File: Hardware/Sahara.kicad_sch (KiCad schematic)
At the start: 21 parts, among them J1 Conn_01x04, SW1 SW_Push, U1 STM32F103CBT6, Y1 8MHz 18 pF, Y2 32.768 7 pF

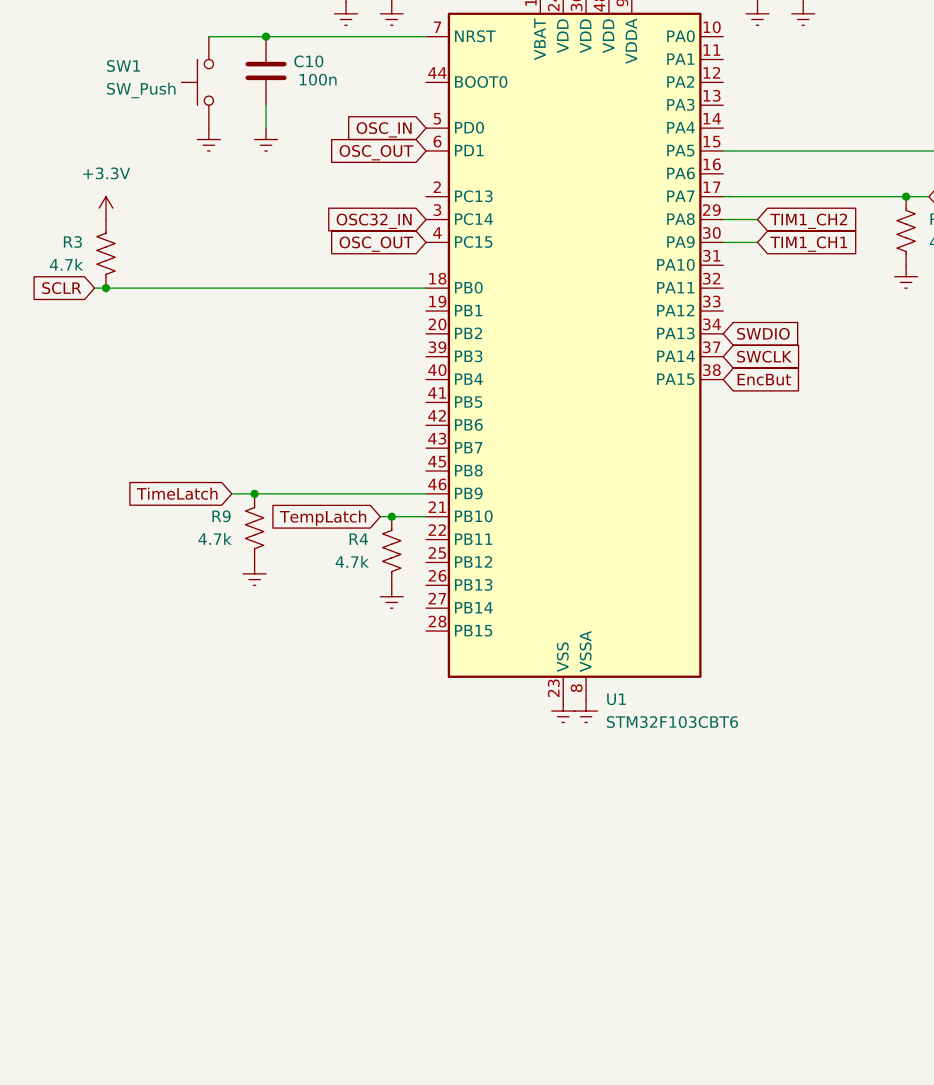
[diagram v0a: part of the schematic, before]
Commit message: schematic update
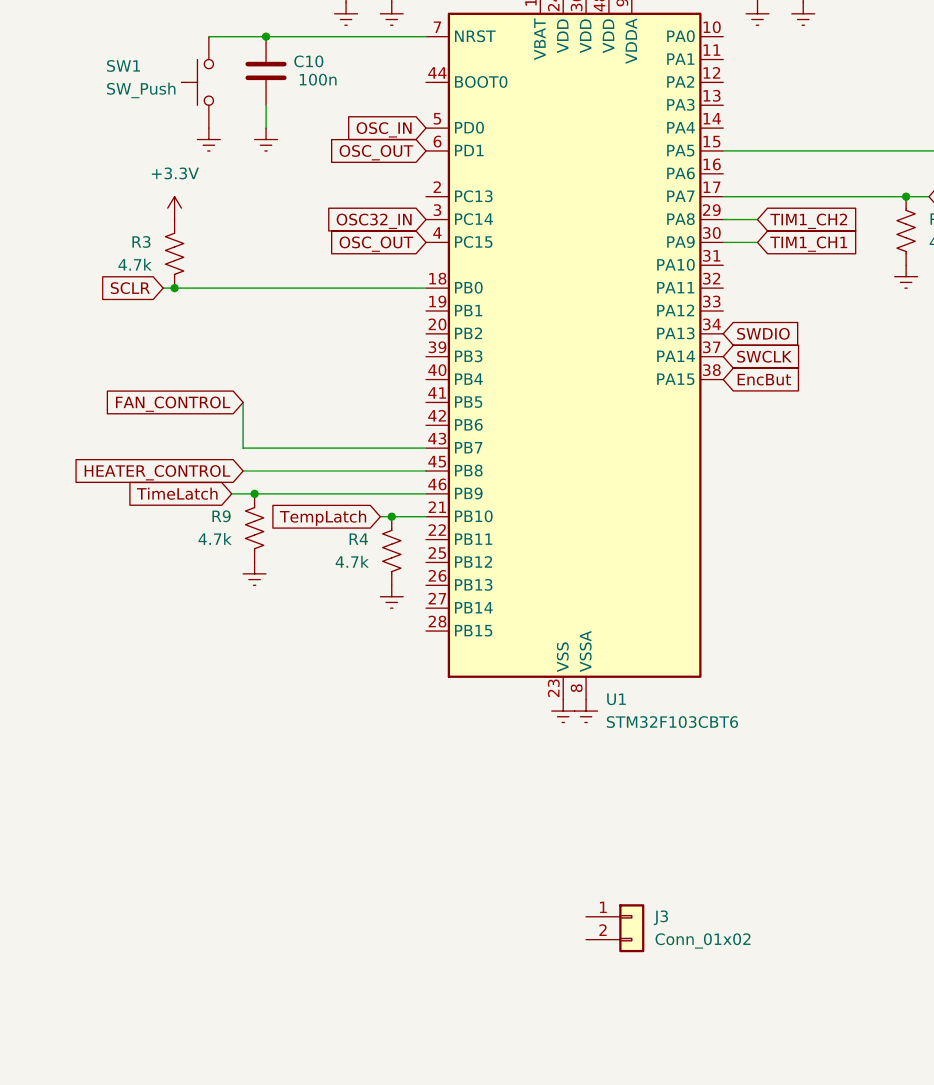
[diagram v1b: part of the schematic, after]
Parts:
- added J3: Conn_01x02, symbol Connector_Generic:Conn_01x02
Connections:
- net FAN_CONTROL: now reaches U1.43 (PB7)
- net HEATER_CONTROL: now reaches U1.45 (PB8)
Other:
- moved on the sheet: R3
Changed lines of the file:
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@@
 	)
 	(junction
-		(at 25.4 76.2)
+		(at 33.02 76.2)
 		(diameter 0)
 		(color 0 0 0 0)
@@
 	(wire
 		(pts
+			(xy 40.64 96.52) (xy 60.96 96.52)
+		)
+		(stroke
+			(width 0)
+			(type default)
+		)
+	)
+	(wire
+		(pts
 			(xy 161.29 30.48) (xy 166.37 30.48)
 		)
@@
 	(wire
 		(pts
-			(xy 24.13 76.2) (xy 25.4 76.2)
+			(xy 31.75 76.2) (xy 33.02 76.2)
 		)
 		(stroke
@@
 	(wire
 		(pts
+			(xy 40.64 93.98) (xy 60.96 93.98)
+		)
+		(stroke
+			(width 0)
+			(type default)
+		)
+	)
+	(wire
+		(pts
 			(xy 166.37 20.32) (xy 177.8 20.32)
 		)
@@
 	(wire
 		(pts
-			(xy 25.4 76.2) (xy 60.96 76.2)
+			(xy 33.02 76.2) (xy 60.96 76.2)
 		)
 		(stroke
@@
 	(wire
 		(pts
+			(xy 40.64 88.9) (xy 40.64 93.98)
+		)
+		(stroke
+			(width 0)
+			(type default)
+		)
+	)
+	(wire
+		(pts
 			(xy 55.88 101.6) (xy 57.15 101.6)
 		)
@@
 	(global_label "SCLR"
 		(shape input)
-		(at 24.13 76.2 180)
+		(at 31.75 76.2 180)
+		(fields_autoplaced yes)
+		(effects
+			(font
+				(size 1.27 1.27)
+			)
+			(justify right)
+		)
+		(property "Intersheetrefs" "${INTERSHEET_REFS}"
+			(at 23.9872 76.2 0)
+			(effects
+				(font
+					(size 1.27 1.27)
+				)
+				(justify right)
+				(hide yes)
+			)
+		)
+	)
+	(global_label "FAN_CONTROL"
+		(shape input)
+		(at 40.64 88.9 180)
 		(fields_autoplaced yes)
 		(effects
@@
 		)
 		(property "Intersheetrefs" "${INTERSHEET_REFS}"
-			(at 16.3672 76.2 0)
+			(at 24.6523 88.9 0)
 			(effects
 				(font
@@
 		)
 	)
+	(global_label "HEATER_CONTROL"
+		(shape input)
+		(at 40.64 96.52 180)
+		(fields_autoplaced yes)
+		(effects
+			(font
+				(size 1.27 1.27)
+			)
+			(justify right)
+		)
+		(property "Intersheetrefs" "${INTERSHEET_REFS}"
+			(at 21.2053 96.52 0)
+			(effects
+				(font
+					(size 1.27 1.27)
+				)
+				(justify right)
+				(hide yes)
+			)
+		)
+	)
 	(global_label "OSC32_IN"
 		(shape input)
@@
 	(symbol
 		(lib_id "Device:R_US")
-		(at 25.4 72.39 0)
+		(at 33.02 72.39 0)
 		(mirror y)
 		(unit 1)
@@
 		(dnp no)
 		(property "Reference" "R3"
-			(at 22.86 71.1199 0)
+			(at 30.48 71.1199 0)
 			(effects
 				(font
@@
 		)
 		(property "Value" "4.7k"
-			(at 22.86 73.6599 0)
+			(at 30.48 73.6599 0)
 			(effects
 				(font
@@
 		)
 		(property "Footprint" ""
-			(at 24.384 72.644 90)
+			(at 32.004 72.644 90)
 			(effects
 				(font
@@
 		)
 		(property "Datasheet" "~"
-			(at 25.4 72.39 0)
+			(at 33.02 72.39 0)
 			(effects
 				(font
@@
 		)
 		(property "Description" "Resistor, US symbol"
-			(at 25.4 72.39 0)
+			(at 33.02 72.39 0)
 			(effects
 				(font
@@
 	(symbol
 		(lib_id "power:+3.3V")
-		(at 25.4 68.58 0)
+		(at 33.02 68.58 0)
 		(unit 1)
 		(exclude_from_sim no)
@@
 		(fields_autoplaced yes)
 		(property "Reference" "#PWR020"
-			(at 25.4 72.39 0)
+			(at 33.02 72.39 0)
 			(effects
 				(font
@@
 		)
 		(property "Value" "+3.3V"
-			(at 25.4 63.5 0)
+			(at 33.02 63.5 0)
 			(effects
 				(font
@@
 		)
 		(property "Footprint" ""
-			(at 25.4 68.58 0)
+			(at 33.02 68.58 0)
 			(effects
 				(font
@@
 		)
 		(property "Datasheet" ""
-			(at 25.4 68.58 0)
+			(at 33.02 68.58 0)
 			(effects
 				(font
@@
 		)
 		(property "Description" "Power symbol creates a global label with name \"+3.3V\""
-			(at 25.4 68.58 0)
+			(at 33.02 68.58 0)
 			(effects
 				(font
@@
 					(unit 1)
 				)
+			)
+		)
+	)
+	(symbol
+		(lib_id "Connector_Generic:Conn_01x02")
+		(at 83.82 146.05 0)
+		(unit 1)
+		(exclude_from_sim no)
+		(in_bom yes)
+		(on_board yes)
+		(dnp no)
+		(fields_autoplaced yes)
+		(property "Reference" "J3"
+			(at 86.36 146.0499 0)
+			(effects
+				(font
+					(size 1.27 1.27)
+				)
+				(justify left)
+			)
+		)
+		(property "Value" "Conn_01x02"
+			(at 86.36 148.5899 0)
+			(effects
+				(font
+					(size 1.27 1.27)
+				)
+				(justify left)
+			)
+		)
+		(property "Footprint" ""
+			(at 83.82 146.05 0)
+			(effects
+				(font
+					(size 1.27 1.27)
+				)
+				(hide yes)
+			)
+		)
+		(property "Datasheet" "~"
+			(at 83.82 146.05 0)
+			(effects
+				(font
+					(size 1.27 1.27)
+				)
+				(hide yes)
+			)
+		)
+		(property "Description" "Generic connector, single row, 01x02, script generated (kicad-library-utils/schlib/autogen/connector/)"
+			(at 83.82 146.05 0)
+			(effects
+				(font
+					(size 1.27 1.27)
+				)
+				(hide yes)
+			)
+		)
+		(pin "1"
+		)
+		(pin "2"
+		)
+		(instances
+			(project ""
+				(path "/1677429e-c497-4bfd-afaa-f24906fcbe1d"
+					(reference "J3")
+					(unit 1)
+				)

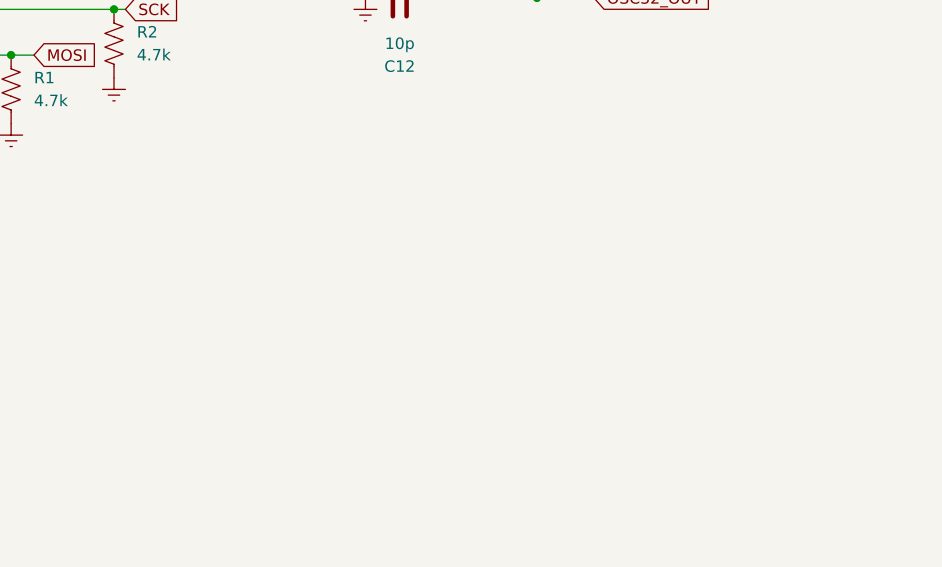
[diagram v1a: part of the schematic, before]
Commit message: Safety features on mains voltage
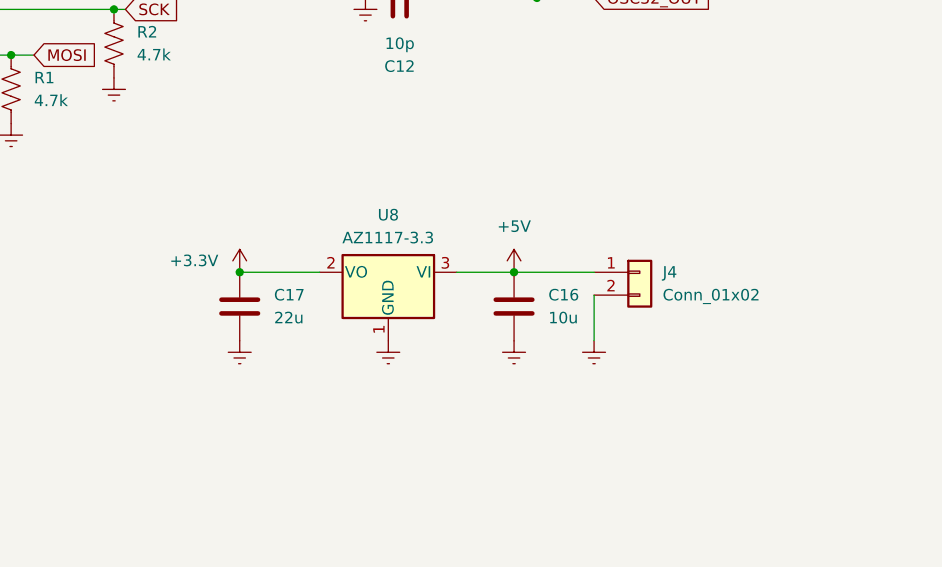
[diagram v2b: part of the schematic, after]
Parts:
- added C16: 10u, symbol Device:C
- added C17: 22u, symbol Device:C
- added J4: Conn_01x02, symbol Connector_Generic:Conn_01x02
- added U8: AZ1117-3.3, symbol Regulator_Linear:AZ1117-3.3
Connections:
- net +3.3V: now also C17.1, U8.2 (VO)
- net Earth: now also C16.2, C17.2, J4.2 (Pin_2), U8.1 (GND)
- new net +5V: C16.1, J4.1 (Pin_1), U8.3 (VI)

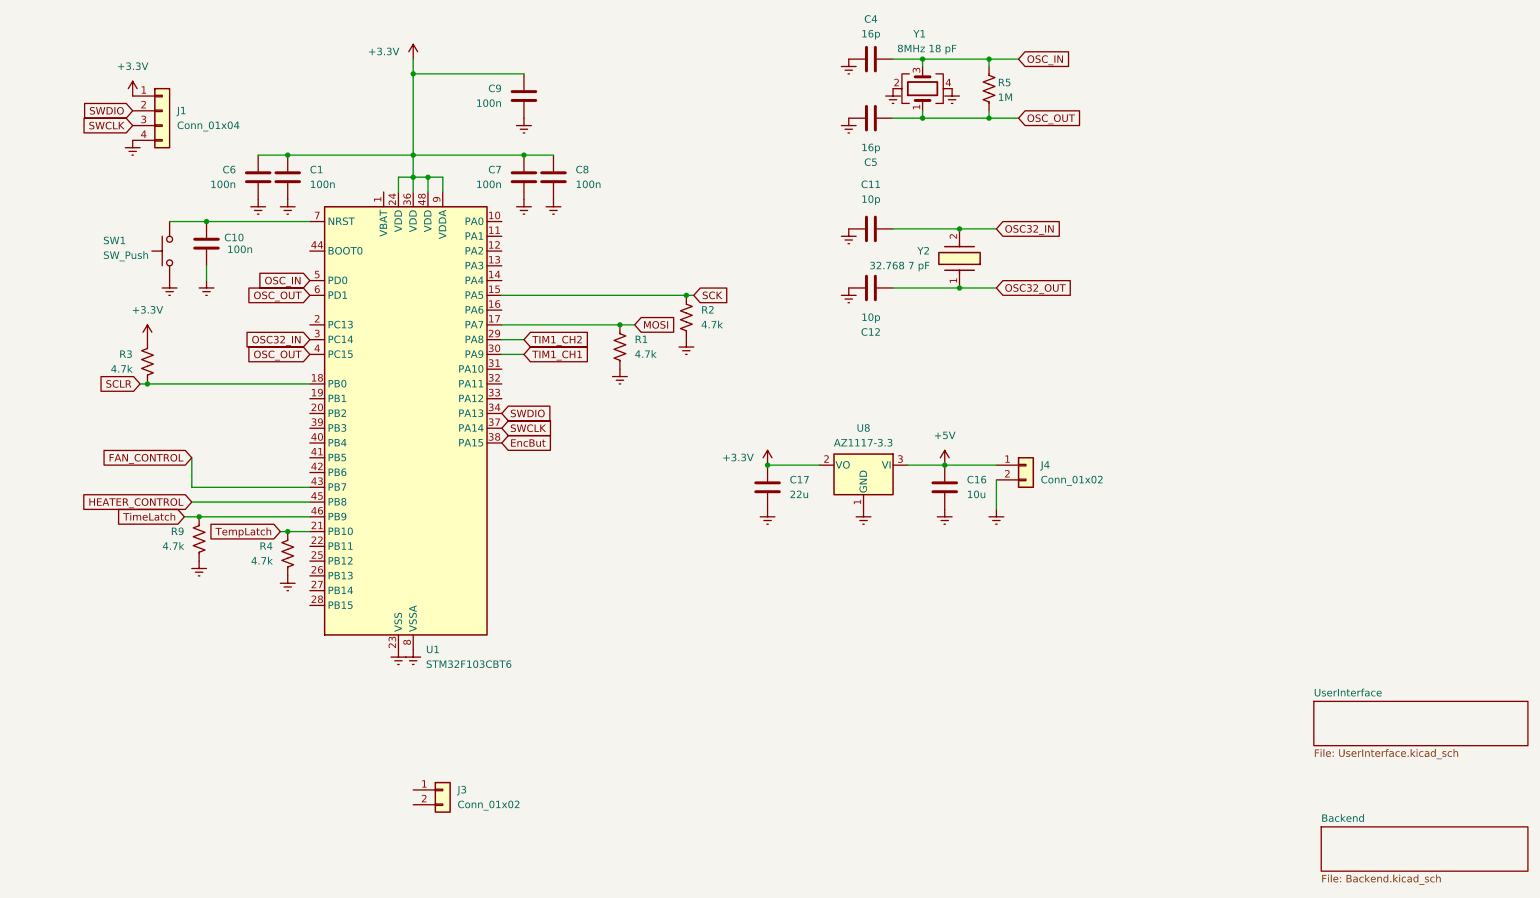
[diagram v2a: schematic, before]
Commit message: added footprints
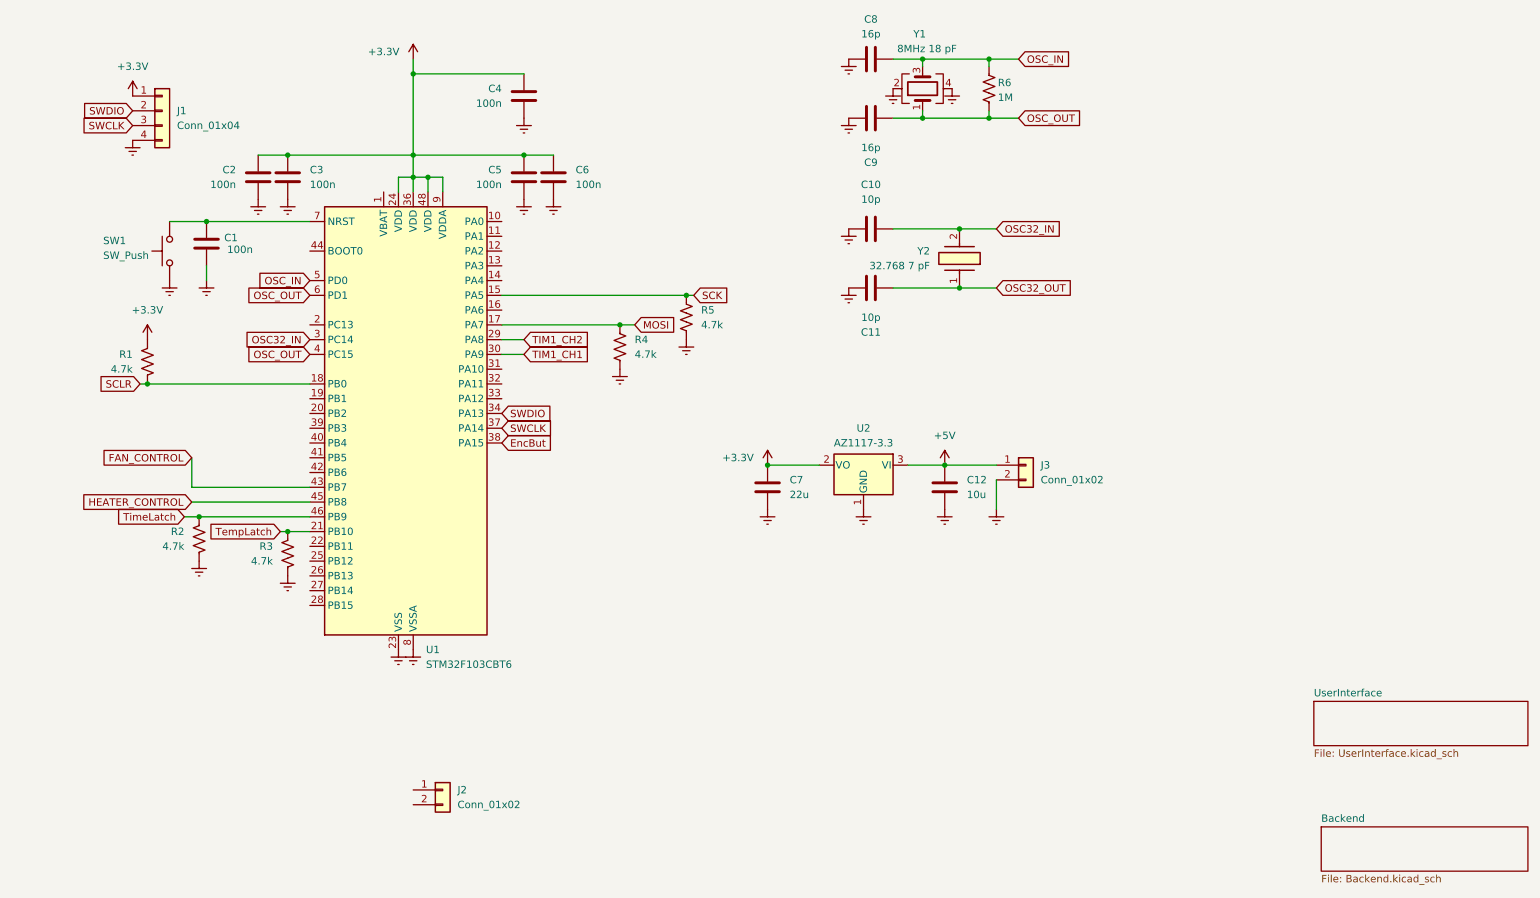
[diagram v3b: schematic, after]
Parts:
- C1: renamed from C10; footprint (none) -> Capacitor_SMD:C_0805_2012Metric
- C10: renamed from C11; footprint (none) -> Capacitor_SMD:C_0805_2012Metric
- C11: renamed from C12; footprint (none) -> Capacitor_SMD:C_0805_2012Metric
- C12: renamed from C16; footprint (none) -> Capacitor_SMD:C_0805_2012Metric
- C2: renamed from C6; footprint (none) -> Capacitor_SMD:C_0805_2012Metric
- C3: renamed from C1; footprint (none) -> Capacitor_SMD:C_0805_2012Metric
- C4: renamed from C9; footprint (none) -> Capacitor_SMD:C_0805_2012Metric
- C5: renamed from C7; footprint (none) -> Capacitor_SMD:C_0805_2012Metric
- C6: renamed from C8; footprint (none) -> Capacitor_SMD:C_0805_2012Metric
- C7: renamed from C17; footprint (none) -> Capacitor_SMD:C_0805_2012Metric
- C8: renamed from C4; footprint (none) -> Capacitor_SMD:C_0805_2012Metric
- C9: renamed from C5; footprint (none) -> Capacitor_SMD:C_0805_2012Metric
- R1: renamed from R3; footprint (none) -> Resistor_SMD:R_0805_2012Metric
- R2: renamed from R9; footprint (none) -> Resistor_SMD:R_0805_2012Metric
- R3: renamed from R4; footprint (none) -> Resistor_SMD:R_0805_2012Metric
- R4: renamed from R1; footprint (none) -> Resistor_SMD:R_0805_2012Metric
- R5: renamed from R2; footprint (none) -> Resistor_SMD:R_0805_2012Metric
- R6: renamed from R5; footprint (none) -> Resistor_SMD:R_0805_2012Metric
- U2: renamed from U8; footprint (none) -> SamacSys_Parts:SOT230P700X180-4N
- renumbered J3 to J2, J4 to J3

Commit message: Added temperature sensor and I2C setup, started PCB layout
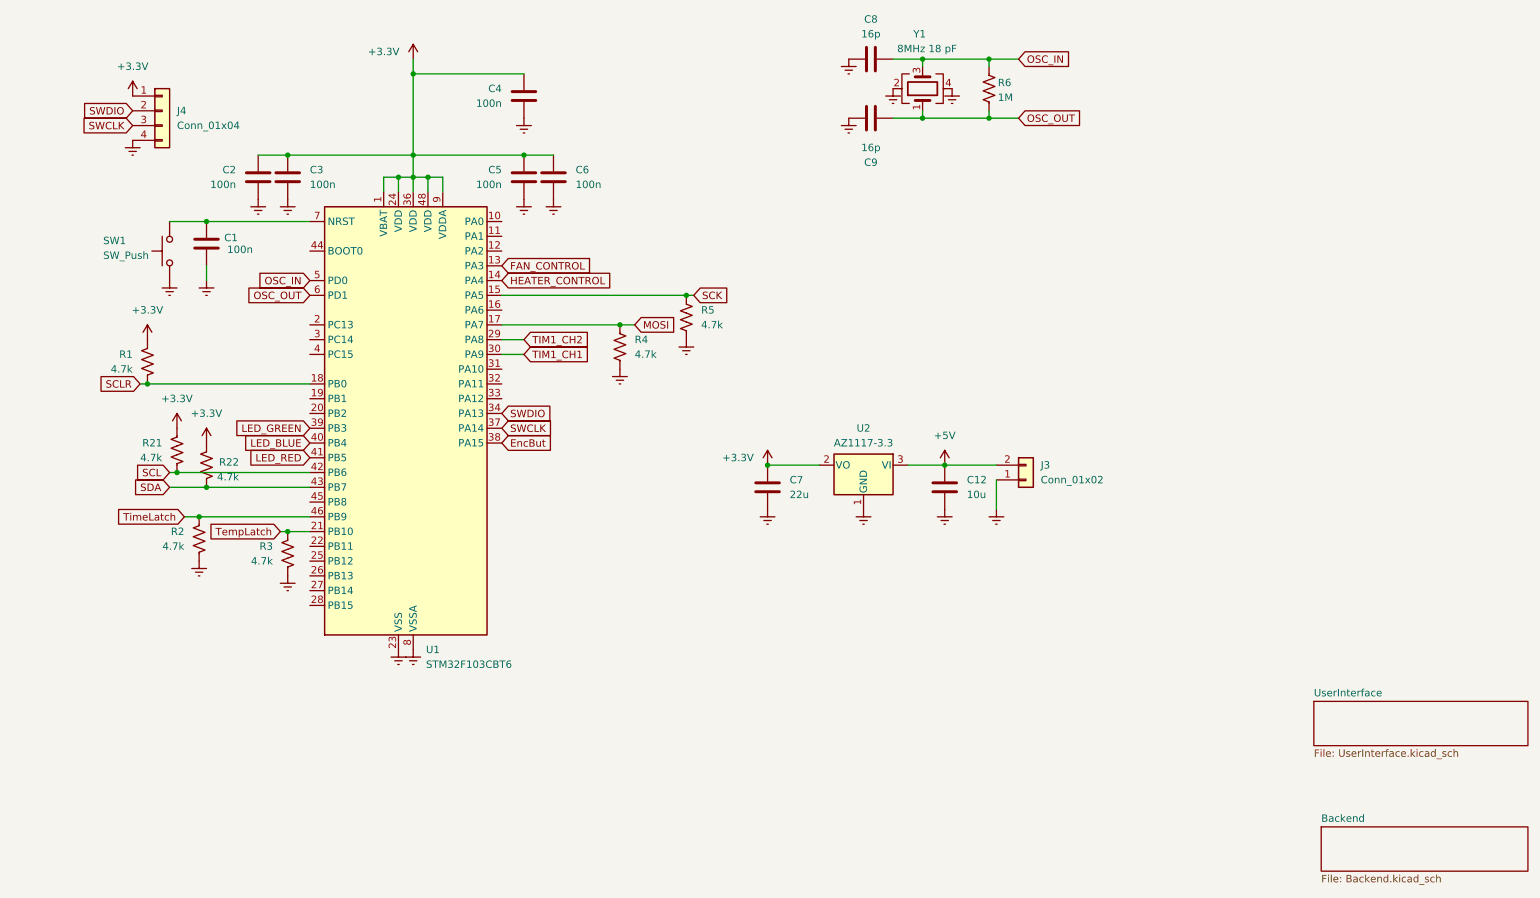
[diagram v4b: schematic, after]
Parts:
- removed C10, C11: 10p, Capacitor_SMD:C_0805_2012Metric, symbol Device:C
- removed J2: Conn_01x02, symbol Connector_Generic:Conn_01x02
- removed Y2: 32.768 7 pF, SamacSys_Parts:SC32S7PF20PPM, symbol SamacSys_Parts:SC32S-7PF20PPM
- added R21, R22: 4.7k, Resistor_SMD:R_0805_2012Metric, symbol Device:R_US
- J3: footprint (none) -> Connector_JST:JST_XH_B2B-XH-AM_1x02_P2.50mm_Vertical
- J4: renamed from J1; footprint (none) -> Connector_JST:JST_XH_B4B-XH-AM_1x04_P2.50mm_Vertical
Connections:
- net +3.3V: now also U1.1 (VBAT), R21.1, R22.1
- net +5V: now also J3.2 (Pin_1); no longer J3.1 (Pin_1)
- net Earth: now also J3.1 (Pin_2); no longer J3.2 (Pin_2)
- net FAN_CONTROL: now also U1.13 (PA3); no longer U1.43 (PB7)
- net HEATER_CONTROL: now also U1.14 (PA4); no longer U1.45 (PB8)
- net OSC_OUT: no longer U1.4 (PC15)
- net LED_GREEN: now reaches U1.39 (PB3)
- net LED_BLUE: now reaches U1.40 (PB4)
- net LED_RED: now reaches U1.41 (PB5)
- net SCL: now reaches U1.42 (PB6)
- net SCL: now also R21.2
- net OSC32_IN: no longer names the net of U1.3 (PC14)
- new net SDA: R22.2, U1.43 (PB7)
